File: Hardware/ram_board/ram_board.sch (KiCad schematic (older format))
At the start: 8 parts, among them J1 Conn_01x40, U1 74LS00, U2 28C256, U3 IDT71256SA15

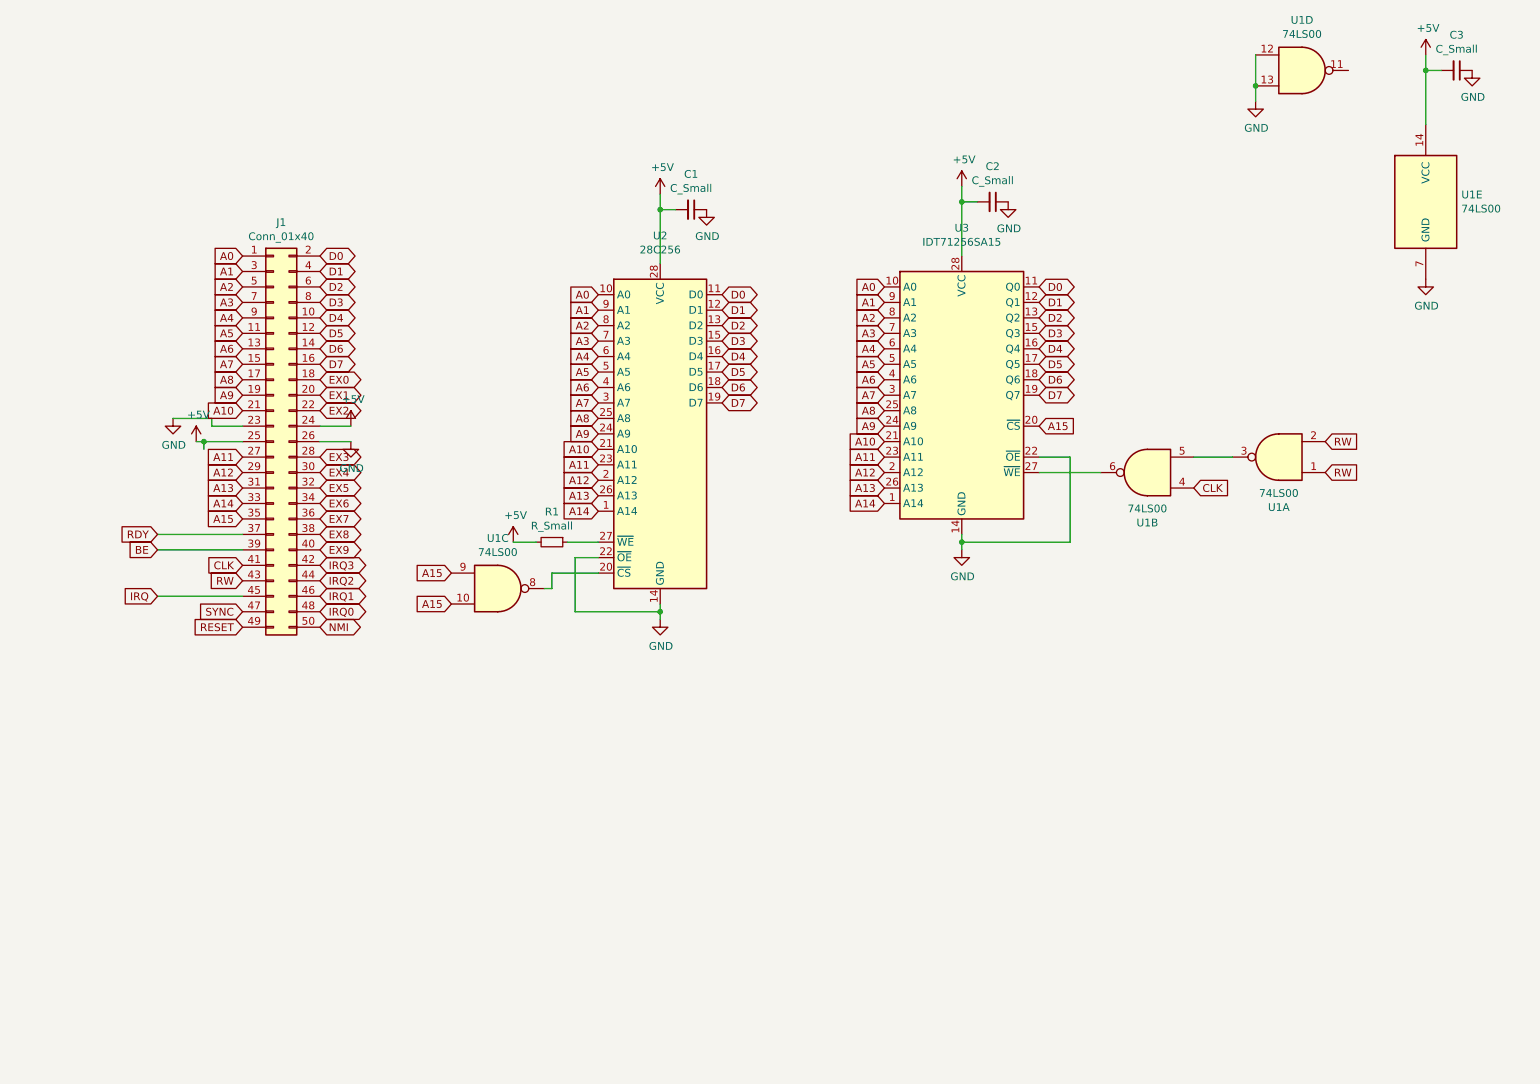
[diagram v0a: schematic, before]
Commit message: 512K RAM board
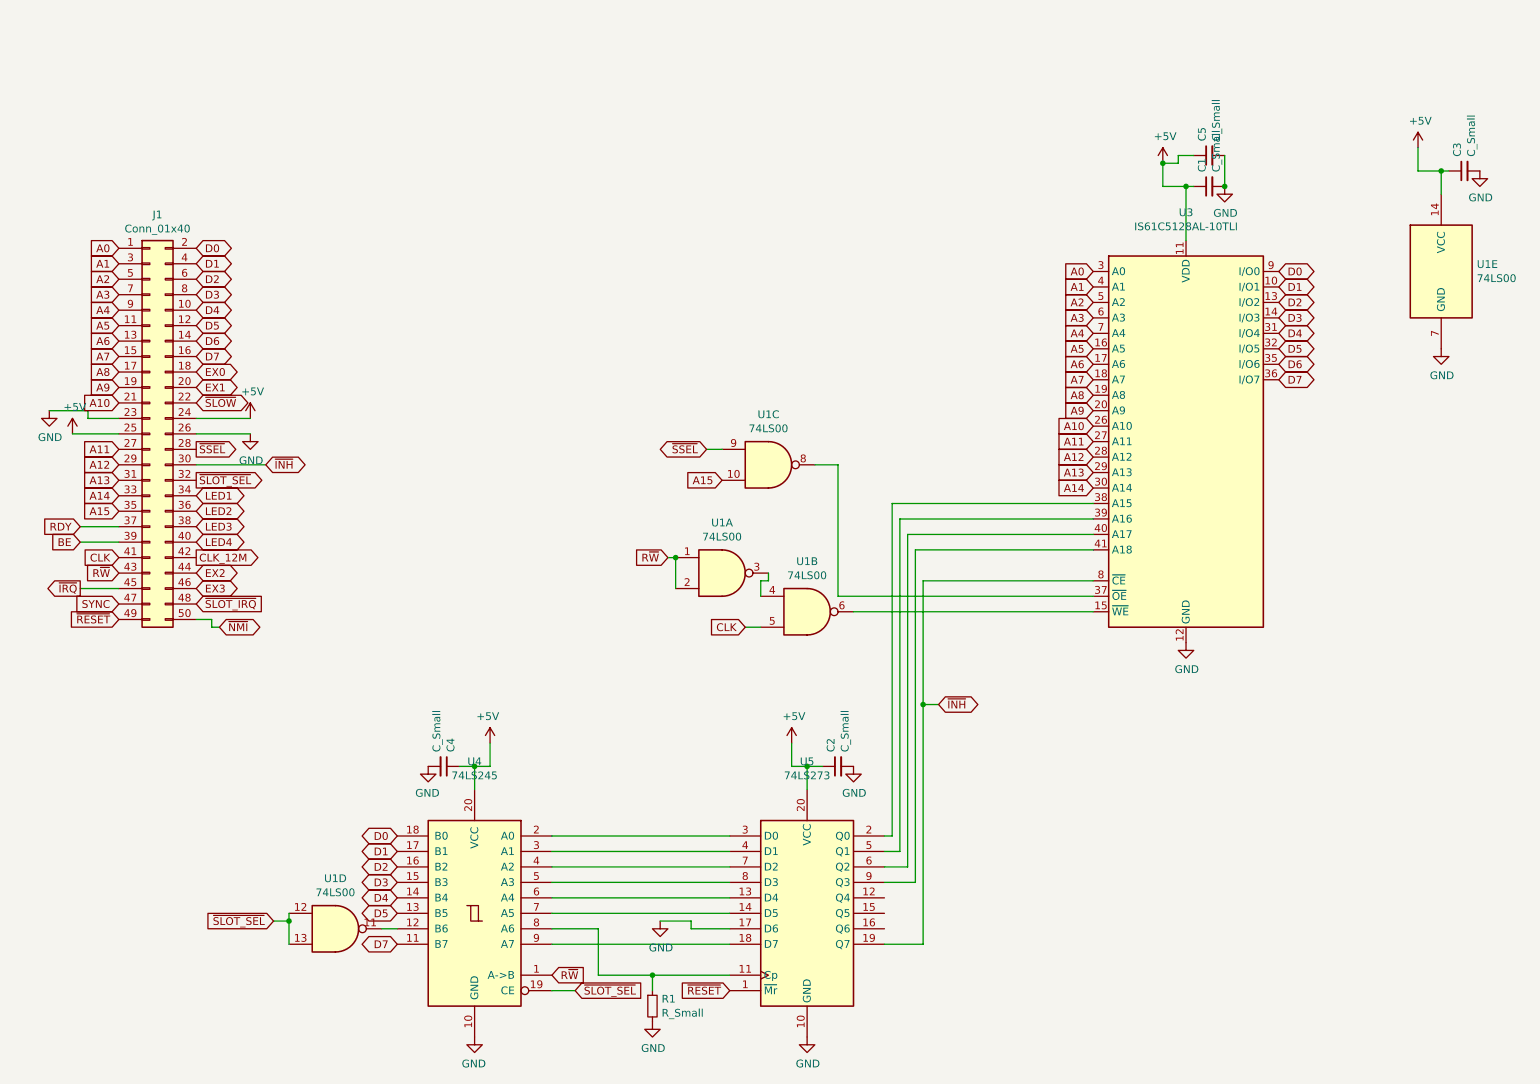
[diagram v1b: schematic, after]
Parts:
- removed U2: 28C256, Package_DIP:DIP-28_W15.24mm_Socket, symbol Memory_EEPROM:28C256
- removed U3: IDT71256SA15, Package_DIP:DIP-28_W7.62mm_Socket, symbol Memory_RAM:HM62256BLP
- added C4, C5: C_Small, Capacitor_THT:C_Disc_D4.3mm_W1.9mm_P5.00mm, symbol Device:C_Small
- added U3: IS61C5128AL-10TLI, Package_SO:TSOP-II-44_10.16x18.41mm_P0.8mm, symbol Memory_RAM:IS61C5128AL-10TLI
- added U4: 74LS245, Package_DIP:DIP-20_W7.62mm_Socket, symbol 74xx:74LS245
- added U5: 74LS273, Package_DIP:DIP-20_W7.62mm_Socket, symbol 74xx:74LS273
- C1, C2, C3: footprint Capacitor_SMD:C_1206_3216Metric_Pad1.42x1.75mm_HandSolder -> Capacitor_THT:C_Disc_D4.3mm_W1.9mm_P5.00mm
- R1: footprint Resistor_SMD:R_0805_2012Metric_Pad1.15x1.40mm_HandSolder -> Resistor_THT:R_Axial_DIN0204_L3.6mm_D1.6mm_P5.08mm_Horizontal
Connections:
- net IRQ1 is gone; now on net EX3: J1.46 (Pin_46)
- net IRQ2 is gone; now on net EX2: J1.44 (Pin_44)
- net +5V: now also C1.1, C2.1, C3.1, C4.1, C5.1, U3.11 (VDD), U3.33 (VDD), U4.20 (VCC), U5.20 (VCC); no longer C1.2, C2.2, C3.2, R1.2
- net A0: now also U3.3 (A0)
- net A1: now also U3.4 (A1)
- net A10: now also U3.26 (A10)
- net A11: now also U3.27 (A11)
- net A12: now also U3.28 (A12)
- net A13: now also U3.29 (A13)
- net A14: now also U3.30 (A14)
- net A15: no longer U1.9
- net A2: now also U3.5 (A2)
- net A3: now also U3.6 (A3)
- net A4: now also U3.7 (A4)
- net A5: now also U3.16 (A5)
- net A6: now also U3.17 (A6)
- net A7: now also U3.18 (A7)
- net A8: now also U3.19 (A8)
- net A9: now also U3.20 (A9)
- net CLK: now also U1.5; no longer U1.4
- net D0: now also U3.9 (I/O0), U4.18 (B0)
- net D1: now also U3.10 (I/O1), U4.17 (B1)
- net D2: now also U3.13 (I/O2), U4.16 (B2)
- net D3: now also U3.14 (I/O3), U4.15 (B3)
- net D4: now also U3.31 (I/O4), U4.14 (B4)
- net D5: now also U3.32 (I/O5), U4.13 (B5)
- net D6: now also U3.35 (I/O6)
- net D7: now also U3.36 (I/O7), U4.11 (B7)
- net EX2: no longer J1.22 (Pin_22)
- net EX3: no longer J1.28 (Pin_28)
- net GND: now also C1.2, C2.2, C3.2, R1.2, C4.2, C5.2, U3.12 (GND), U3.34 (GND), U4.10 (GND), U5.10 (GND), U5.17 (D6); no longer C1.1, C2.1, C3.1, U1.12, U1.13
- net at U1.8: now also U3.37 (~OE)
- net at R1.1: now also U4.8 (A6), U5.11 (Cp)
- net at U1.6: now also U3.15 (~WE)
- net at U1.3: now also U1.4; no longer U1.5
- net at U1.11: now also U4.12 (B6)
- net EX4 renamed ~INH~
- net ~INH~: now also U3.8 (~CE), U5.19 (Q7)
- net EX5 renamed ~SLOT_SEL~
- net ~SLOT_SEL~: now also U1.12, U1.13, U4.19 (CE)
- net EX6 renamed LED1
- net EX7 renamed LED2
- net EX8 renamed LED3
- net EX9 renamed LED4
- net IRQ renamed ~IRQ~
- net IRQ0 renamed ~SLOT_IRQ~
- net IRQ3 renamed CLK_12M
- net NMI renamed ~NMI~
- net RESET renamed ~RESET~
- net ~RESET~: now also U5.1 (~Mr)
- net RW renamed R~W~
- net R~W~: now also U4.1 (A->B)
- new net: U3.38 (A15), U5.2 (Q0)
- new net: U3.39 (A16), U5.5 (Q1)
- new net: U3.40 (A17), U5.6 (Q2)
- new net: U3.41 (A18), U5.9 (Q3)
- new net: U4.6 (A4), U5.13 (D4)
- new net: U4.7 (A5), U5.14 (D5)
- new net: U4.9 (A7), U5.18 (D7)
- new net: U4.2 (A0), U5.3 (D0)
- new net: U4.3 (A1), U5.4 (D1)
- new net: U4.4 (A2), U5.7 (D2)
- new net: U4.5 (A3), U5.8 (D3)
- new net ~SLOW~: J1.22 (Pin_22)
- new net ~SSEL~: J1.28 (Pin_28), U1.9
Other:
- moved on the sheet: J1

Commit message: update footprints on planned RAM expansion board
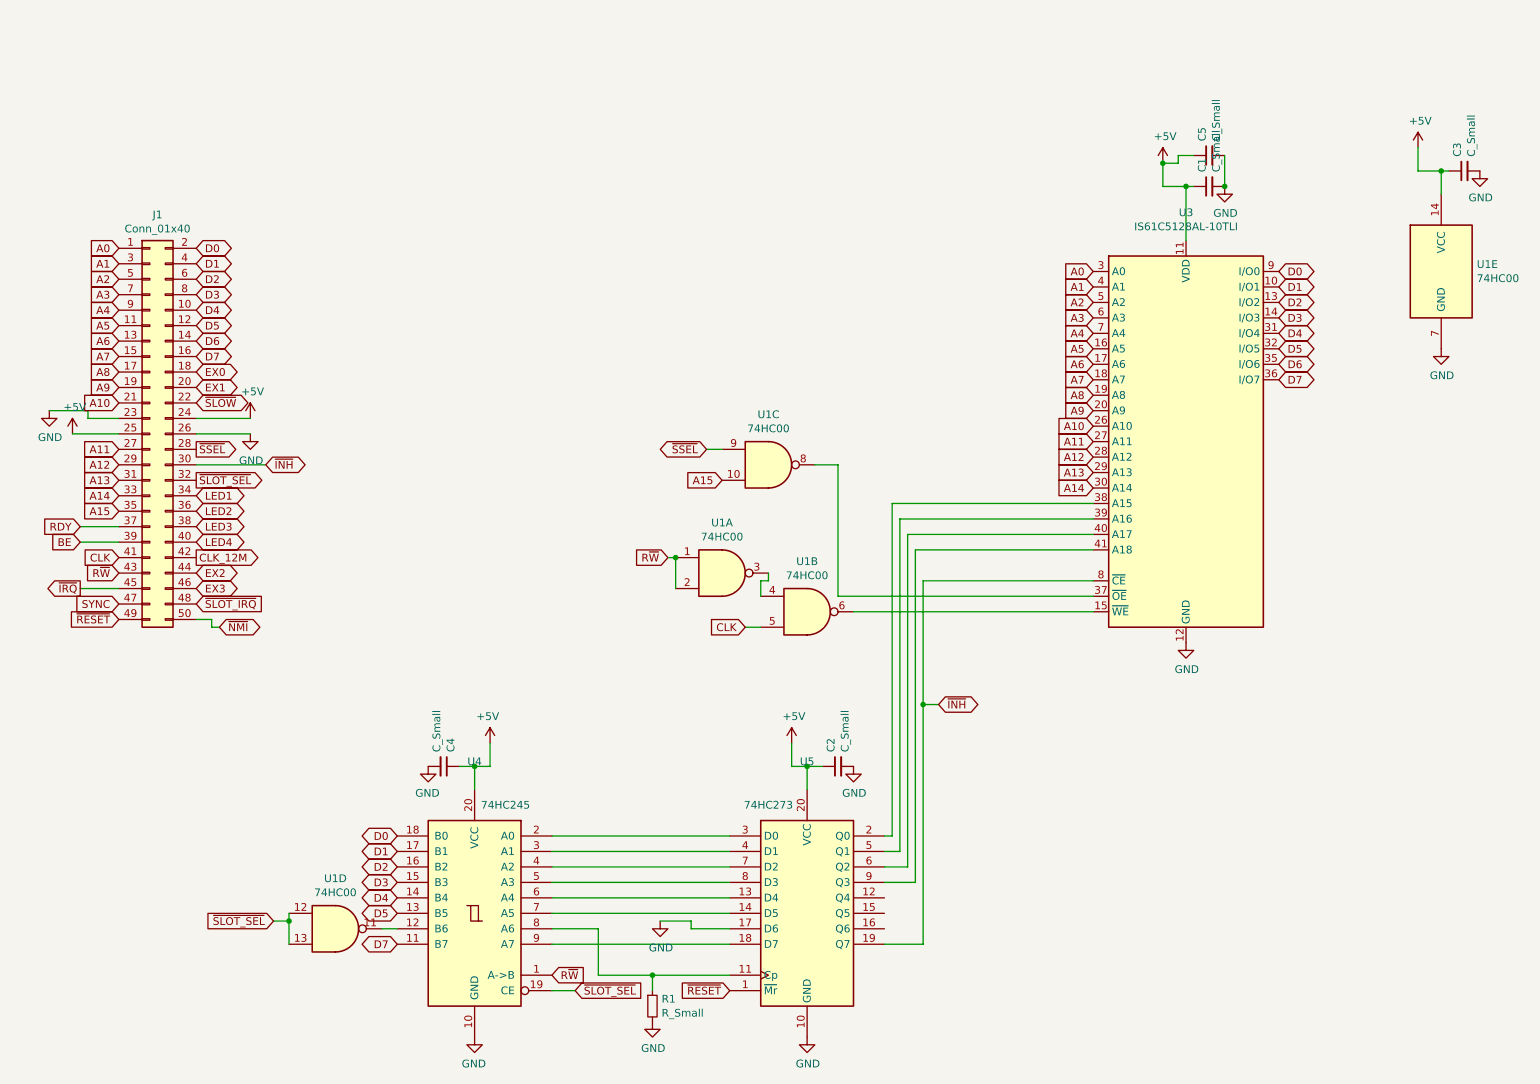
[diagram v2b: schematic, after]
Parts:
- R1: footprint Resistor_THT:R_Axial_DIN0204_L3.6mm_D1.6mm_P5.08mm_Horizontal -> Resistor_THT:R_Axial_DIN0207_L6.3mm_D2.5mm_P7.62mm_Horizontal
- U1: value 74LS00 -> 74HC00
- U4: value 74LS245 -> 74HC245
- U5: value 74LS273 -> 74HC273
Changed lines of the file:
@@
 P 5400 4300
 F 0 "U1" H 5400 4625 50  0000 C CNN
-F 1 "74LS00" H 5400 4534 50  0000 C CNN
+F 1 "74HC00" H 5400 4534 50  0000 C CNN
 F 2 "Package_DIP:DIP-14_W7.62mm_Socket" H 5400 4300 50  0001 C CNN
 F 3 "http://www.ti.com/lit/gpn/sn74ls00" H 5400 4300 50  0001 C CNN
@@
 P 5950 4550
 F 0 "U1" H 5950 4875 50  0000 C CNN
-F 1 "74LS00" H 5950 4784 50  0000 C CNN
+F 1 "74HC00" H 5950 4784 50  0000 C CNN
 F 2 "Package_DIP:DIP-14_W7.62mm_Socket" H 5950 4550 50  0001 C CNN
 F 3 "http://www.ti.com/lit/gpn/sn74ls00" H 5950 4550 50  0001 C CNN
@@
 P 5700 3600
 F 0 "U1" H 5700 3925 50  0000 C CNN
-F 1 "74LS00" H 5700 3834 50  0000 C CNN
+F 1 "74HC00" H 5700 3834 50  0000 C CNN
 F 2 "Package_DIP:DIP-14_W7.62mm_Socket" H 5700 3600 50  0001 C CNN
 F 3 "http://www.ti.com/lit/gpn/sn74ls00" H 5700 3600 50  0001 C CNN
@@
 P 10050 2350
 F 0 "U1" H 10280 2396 50  0000 L CNN
-F 1 "74LS00" H 10280 2305 50  0000 L CNN
+F 1 "74HC00" H 10280 2305 50  0000 L CNN
 F 2 "Package_DIP:DIP-14_W7.62mm_Socket" H 10050 2350 50  0001 C CNN
 F 3 "http://www.ti.com/lit/gpn/sn74ls00" H 10050 2350 50  0001 C CNN
@@
 P 5950 6500
 F 0 "U5" H 5950 7481 50  0000 C CNN
-F 1 "74LS273" H 5950 7390 50  0000 C CNN
+F 1 "74HC273" H 5700 7200 50  0000 C CNN
 F 2 "Package_DIP:DIP-20_W7.62mm_Socket" H 5950 6500 50  0001 C CNN
 F 3 "http://www.ti.com/lit/gpn/sn74LS273" H 5950 6500 50  0001 C CNN
@@
 P 3800 6500
 F 0 "U4" H 3800 7481 50  0000 C CNN
-F 1 "74LS245" H 3800 7390 50  0000 C CNN
+F 1 "74HC245" H 3600 7200 50  0000 C CNN
 F 2 "Package_DIP:DIP-20_W7.62mm_Socket" H 3800 6500 50  0001 C CNN
 F 3 "http://www.ti.com/lit/gpn/sn74LS245" H 3800 6500 50  0001 C CNN
@@
 P 2900 6600
 F 0 "U1" H 2900 6925 50  0000 C CNN
-F 1 "74LS00" H 2900 6834 50  0000 C CNN
+F 1 "74HC00" H 2900 6834 50  0000 C CNN
 F 2 "Package_DIP:DIP-14_W7.62mm_Socket" H 2900 6600 50  0001 C CNN
 F 3 "http://www.ti.com/lit/gpn/sn74ls00" H 2900 6600 50  0001 C CNN
@@
 F 0 "R1" H 5009 7146 50  0000 L CNN
 F 1 "R_Small" H 5009 7055 50  0000 L CNN
-F 2 "Resistor_THT:R_Axial_DIN0204_L3.6mm_D1.6mm_P5.08mm_Horizontal" H 4950 7100 50  0001 C CNN
+F 2 "Resistor_THT:R_Axial_DIN0207_L6.3mm_D2.5mm_P7.62mm_Horizontal" H 4950 7100 50  0001 C CNN
 F 3 "~" H 4950 7100 50  0001 C CNN
 	1    4950 7100
